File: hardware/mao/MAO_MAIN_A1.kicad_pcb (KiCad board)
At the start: 4 copper layers, 58 x 56 mm, 137 parts, among them J101 USB-C, J102 BAT, J201 TAG, J301 LCD, J501 LRA, Q101 AO3401A, Q302 DMG2302UK, Q501 AO3400A, SW301 SKQGADE010, U101 TPD2E2U06, U102 BQ25185DLHR, U103 MAX17048G+T10, U104 TPS62840DLCR, U105 TPS22916CYFPR, U201 ESP32-S3-MINI-1-N8, U301 DRV5012AEDMRR, U302 DRV5012AEDMRR, U304 TLV9061IDBVR, U401 ICM-42670-P, U402 VL53L4CDV0DH/1, U501 MAX98357AETE+T, U502 DRV2605LDGSR, U503 IRM-H638T/TR2, U504 TPS22916CYFPR

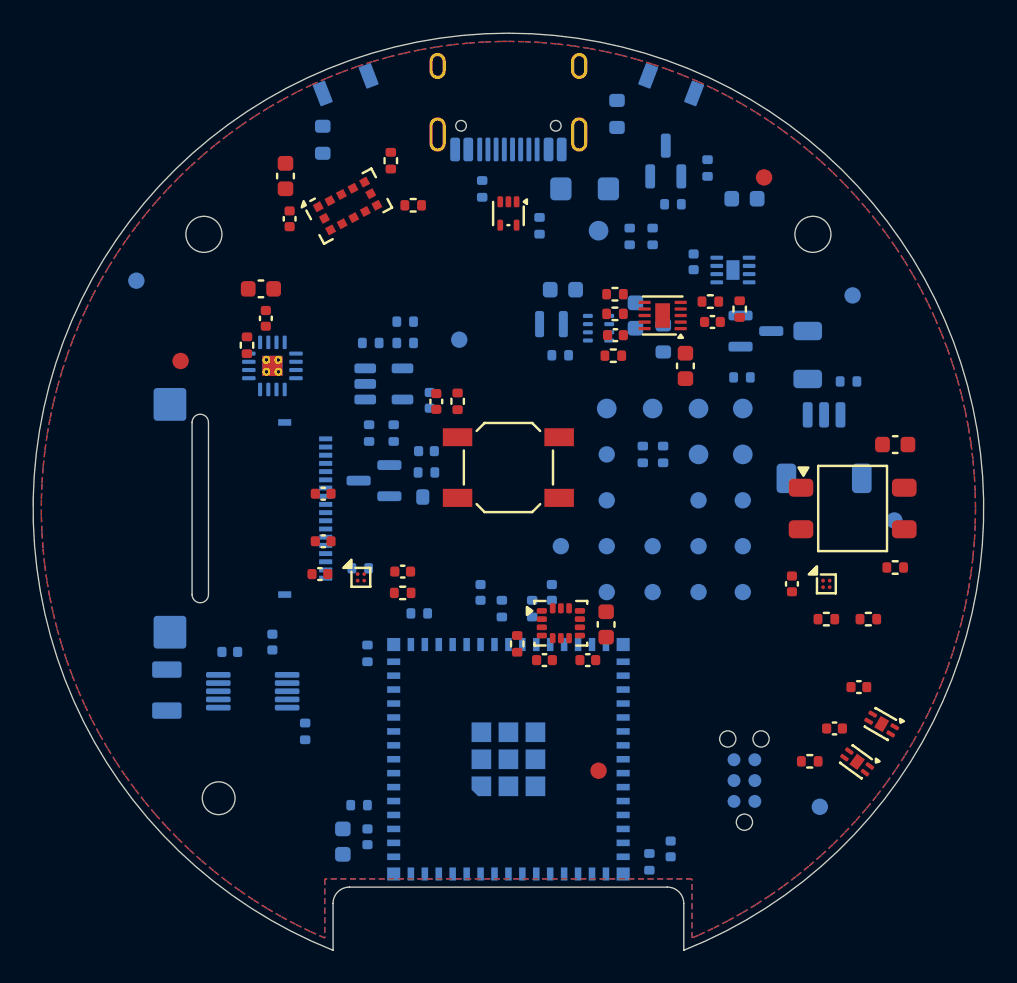
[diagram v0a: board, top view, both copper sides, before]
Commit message: A1 designed copper and rules: BQ25185/TPS62840 power section, VSYS L3 band, A0 copper kept where parts kept
route_power.py / route_local.py rewritten for A1: the buck's input loop, switch node, COUT and VOS sense,
charger SYS to LINK_REG and the L3 VSYS band through two vias, the VSYS via at each load; A0's copper stays for
the USB-C entry, battery chain, speaker, LRA, IR LEDs, ToF, gauge, Hall pair, IR receiver, haptic driver and
service-field pull-ups. power_regions.py: new VSYS band (no 9 o'clock run: the haptic driver is on +3V3) and
+3V3 cores; netrules/project: A1 nets and classes. DRC on the unrouted board: 0 clearance findings.

Co-Authored-By: Claude Opus 5.5 <noreply@anthropic.com>
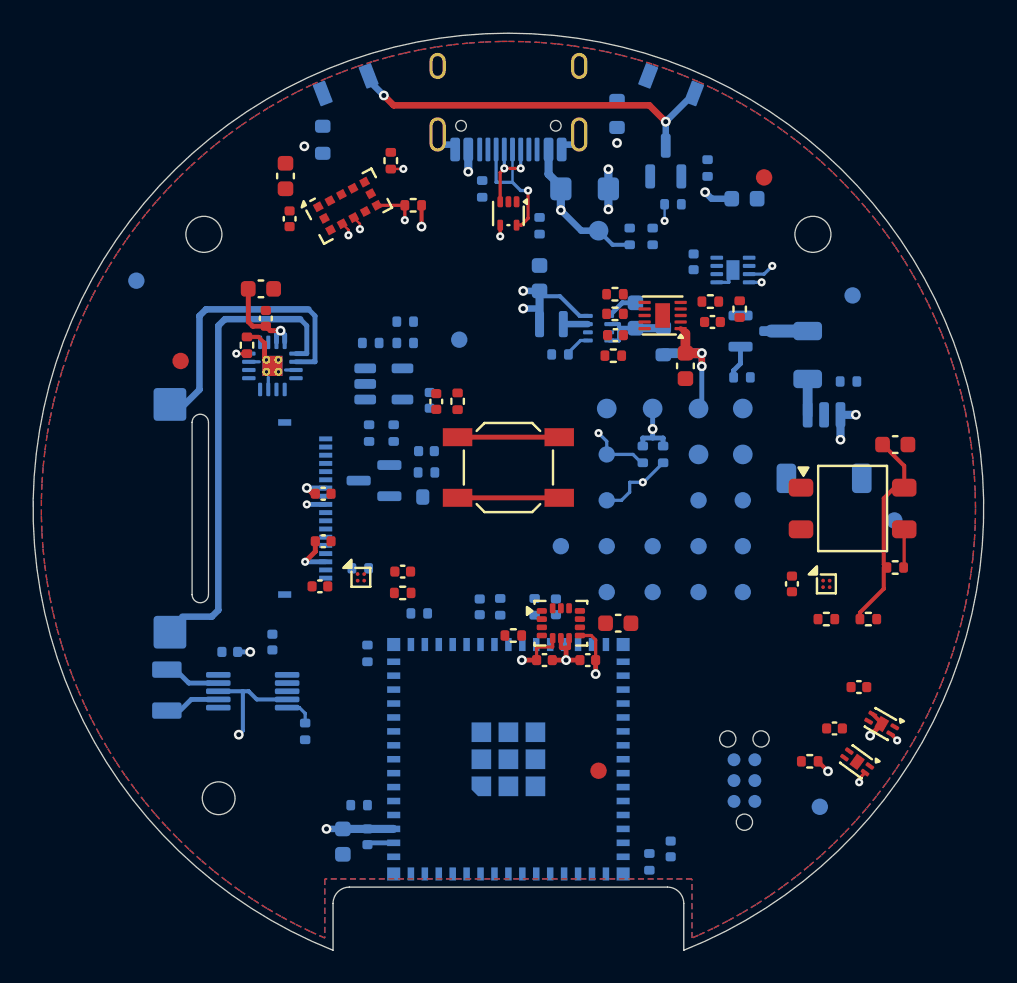
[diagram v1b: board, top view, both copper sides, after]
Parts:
- moved C106 1.59 mm to (51.9, 36.0), turned to 90 degrees
- moved C206 0.91 mm to (52.9, 56.0)
- moved C207 0.88 mm to (48.2, 56.0)
- moved C109 0.75 mm to (38.5, 54.8)
- moved C408 0.74 mm to (56.7, 57.0), turned to 0 degrees
- moved R404 0.56 mm to (50.3, 57.8), turned to 0 degrees
- moved R215 0.19 mm to (51.6, 56.0), turned to -90 degrees
- moved R122 0.17 mm to (59.5, 39.8)
- moved R216 0.15 mm to (49.5, 56.0), turned to -90 degrees
- moved R111 0.05 mm to (53.1, 40.6), turned to 180 degrees
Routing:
- net GND: track 0.00 -> 37.6 mm, vias 0 -> 11
- net SPK_P: track 0.00 -> 27.8 mm
- net +3V3: track 0.00 -> 23.0 mm, vias 0 -> 7
- net IR_LED_K: track 0.00 -> 21.8 mm, vias 0 -> 2
- net VSYS: track 0.00 -> 18.7 mm, vias 0 -> 7
- net SPK_N: track 0.00 -> 17.3 mm
- net IR_RX_VCC: track 0.00 -> 12.2 mm
- net VBUS: track 0.00 -> 9.68 mm, vias 0 -> 2
- net USB_C_DN: track 0.00 -> 7.53 mm, vias 0 -> 1
- net I2C_SCL: track 0.00 -> 6.40 mm, vias 0 -> 3
- net I2C_SDA: track 0.00 -> 6.37 mm, vias 0 -> 3
- net PRESS_N: track 0.00 -> 6.20 mm
- net REG_IN: track 0.00 -> 4.90 mm
- net USB_C_DP: track 0.00 -> 4.24 mm, vias 0 -> 2
- net LRA_N: track 0.00 -> 2.87 mm
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
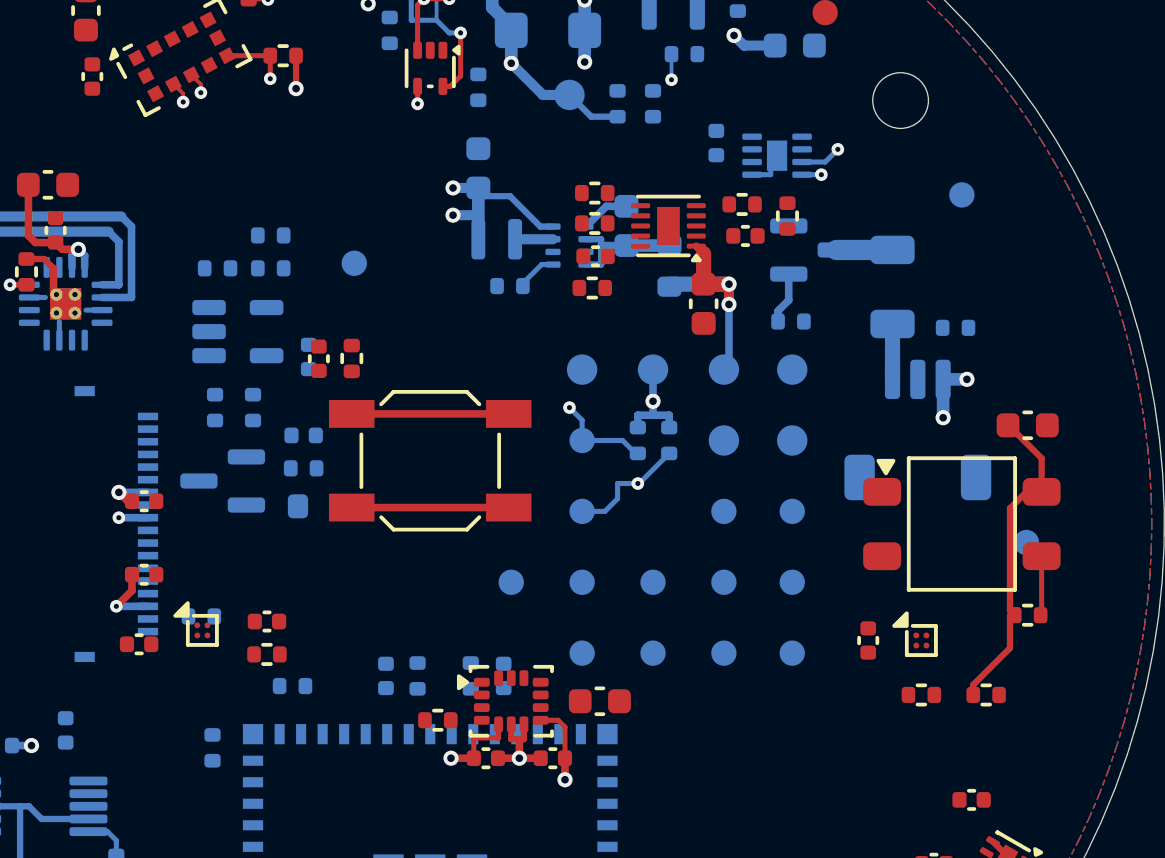
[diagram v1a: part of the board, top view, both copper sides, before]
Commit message: A1 charger fan-out designed (WSON-10 0.4 mm pitch), VBAT chain on B, VSYS strip; A1 power budget
The router could not fan out the BQ25185's 0.4 mm pins: every charger pin now reaches its part on designed
copper, VBAT goes through two vias to Q101, the gauge and TP5 on B, VSYS through two vias to LINK_REG, TP4 and
the L3 band. docs/hardware/mao-power-budget.md is the A1 budget: deep sleep 33.6 uA typ / 66 uA all-max,
+3V3 worst case 543 mA (688 mA by the S3 supply rule) against 750 mA, low-battery floor with the TPS62840 in
100 % mode and Q1's drop.

Co-Authored-By: Claude Opus 5.5 <noreply@anthropic.com>
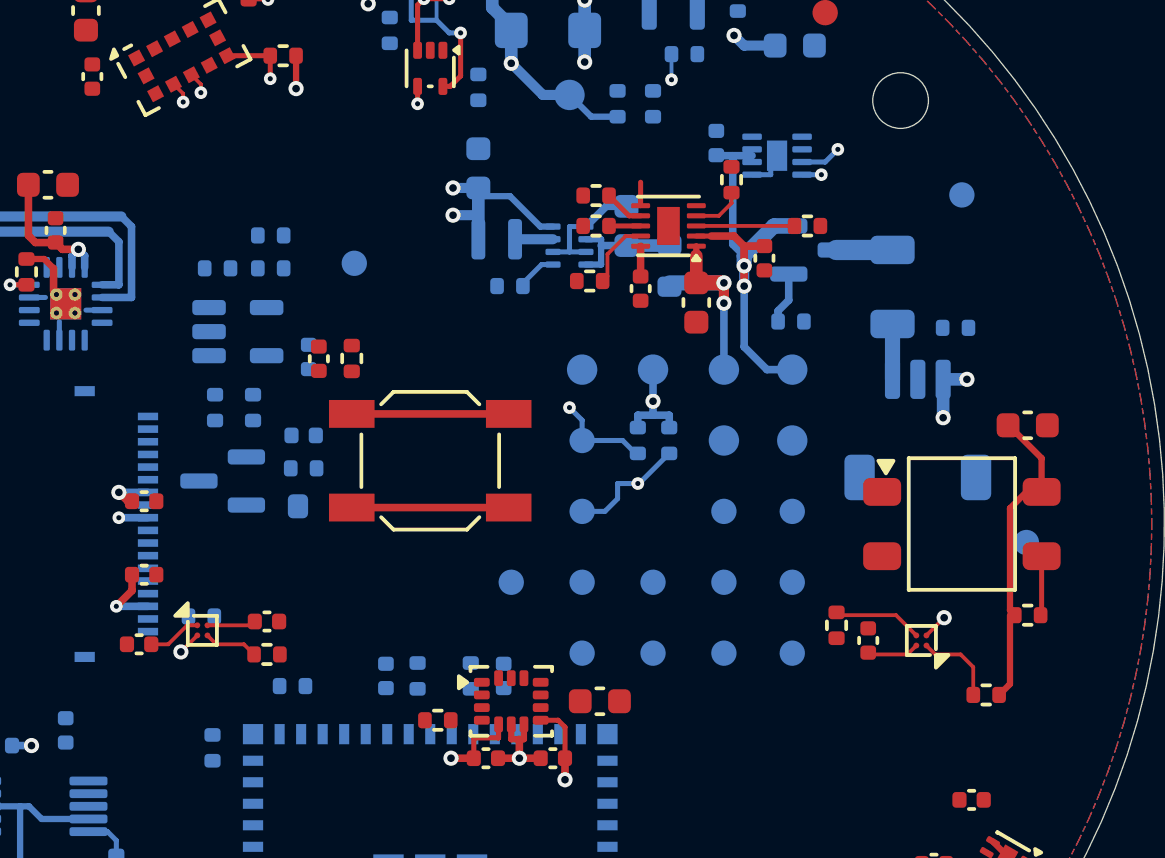
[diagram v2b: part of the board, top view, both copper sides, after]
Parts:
- moved R211 4.33 mm to (66.0, 54.0), turned to -90 degrees
- moved C101 2.19 mm to (58.3, 40.7), turned to -90 degrees
- moved C103 1.16 mm to (63.2, 39.5), turned to -90 degrees
- moved R117 1.06 mm to (61.9, 36.4), turned to 90 degrees
- moved R119 0.88 mm to (64.9, 38.2), turned to 180 degrees
- moved C102 0.29 mm to (60.5, 41.2)
- moved R118 0.29 mm to (56.3, 40.4)
- moved R103 0.11 mm to (56.5, 38.2)
- moved R104 0.11 mm to (56.5, 37.0)
- turned R505 to 0 degrees
- turned U504 to 180 degrees
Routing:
- net VBAT: track 0.00 -> 18.1 mm, vias 0 -> 2
- net GND: track 37.6 -> 42.5 mm, vias 11 -> 13
- net CHG_STAT2: track 0.00 -> 3.88 mm
- net +3V3: track 23.0 -> 26.8 mm
- net AUX_PWR_EN: track 0.00 -> 3.48 mm
- net AUX_3V3: track 0.00 -> 3.30 mm
- net CHG_STAT1: track 0.00 -> 2.74 mm
- net LCD_PWR_EN: track 0.00 -> 2.15 mm
- net 3V3_LCD: track 2.76 -> 4.79 mm
- net CHG_CE_N: track 0.00 -> 2.01 mm
- net CHG_ILIM: track 0.00 -> 1.58 mm
- net CHG_ISET: track 0.00 -> 1.25 mm
- net VBUS: track 9.68 -> 10.9 mm
- net BAT_NTC: track 0.00 -> 0.92 mm

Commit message: A1 layout: module escape vias, J301 DC/TE/RST vias, fixture pads on their nets, BOOT pull-up on F
The first routing pass left 17 connections open around the module: the pin map sends I2S, TE and the dial
across the board, so the crossing pins now leave through staggered escape vias (F and L3 open to the router),
J301's DC/TE/RST drop through vias east of their pads, the display-lane L3 core is gone, and the Gate C fixture
pads sit on their own nets' paths instead of walling off the module's top row. No pin assignment changed.

Co-Authored-By: Claude Opus 5.5 <noreply@anthropic.com>
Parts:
- R202: moved to F.Cu
- moved TP18 26.8 mm to (35.0, 35.7)
- moved TP23 19.4 mm to (59.4, 35.7)
- moved TP17 16.4 mm to (47.0, 37.1)
- moved TP20 14.0 mm to (47.6, 52.4)
- moved TP24 10.3 mm to (51.4, 53.8)
- moved TP25 10.2 mm to (54.2, 53.8)
- moved TP21 9.74 mm to (69.4, 60.6)
- moved R207 9.10 mm to (40.9, 62.8), turned to 180 degrees
- moved TP22 8.76 mm to (64.3, 52.3)
- moved TP19 5.18 mm to (59.7, 57.4)
- moved R202 0.67 mm to (40.6, 68.7)
- moved C301 0.60 mm to (38.1, 52.0)
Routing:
- net LCD_RST_N: track 0.00 -> 3.89 mm, vias 0 -> 1
- net LCD_TE: track 0.00 -> 2.80 mm, vias 0 -> 2
- net LCD_BL_K: track 0.00 -> 2.40 mm
- net LCD_BL: track 0.00 -> 2.00 mm, vias 0 -> 1
- net IMU_INT1: track 0.00 -> 2.00 mm, vias 0 -> 1
- net AMP_DIN: track 0.00 -> 2.00 mm, vias 0 -> 1
- net AMP_BCLK: track 0.00 -> 2.00 mm, vias 0 -> 1
- net LCD_DC: track 0.00 -> 2.00 mm, vias 0 -> 2
- net BOOT: track 0.00 -> 1.89 mm, vias 0 -> 1
- net I2C_SCL: track 6.40 -> 8.06 mm, vias 3 -> 4
- net I2C_SDA: track 6.37 -> 7.96 mm, vias 3 -> 4
- net PRESS_N: track 6.20 -> 7.40 mm, vias 0 -> 1
- net AMP_SD: track 1.41 -> 2.61 mm, vias 1 -> 2
- net AMP_LRCLK: track 0.00 -> 1.20 mm, vias 0 -> 1
- net IR_TX: track 1.01 -> 2.06 mm, vias 1 -> 2

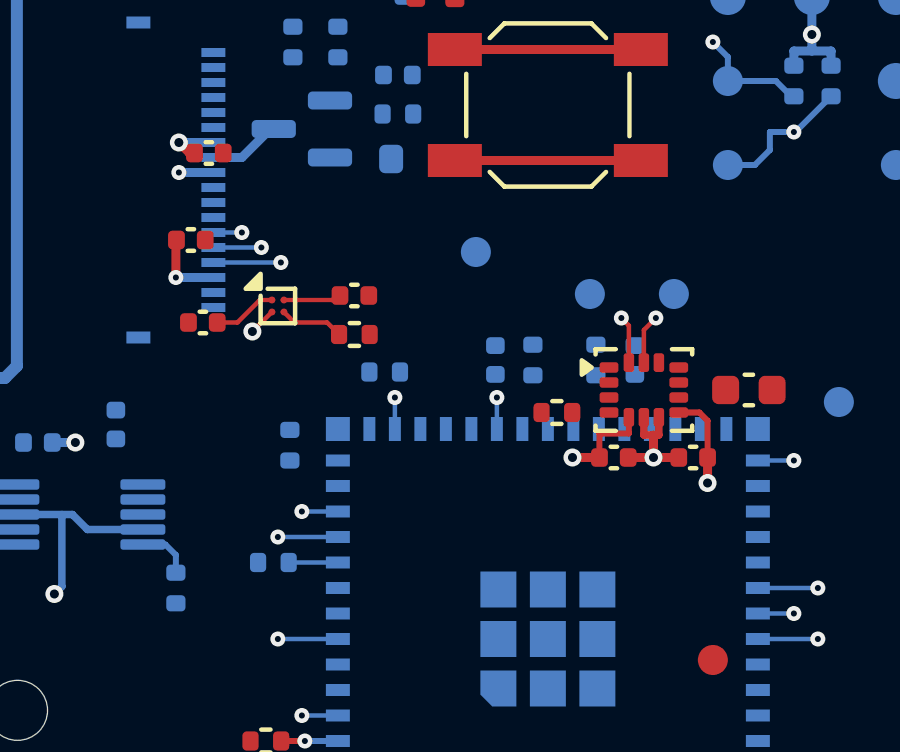
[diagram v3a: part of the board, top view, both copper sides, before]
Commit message: A1 layout: SPI pads of J301 drop to F, USB 22R on F over the module, spare-GPIO pads open
Co-Authored-By: Claude Opus 5.5 <noreply@anthropic.com>
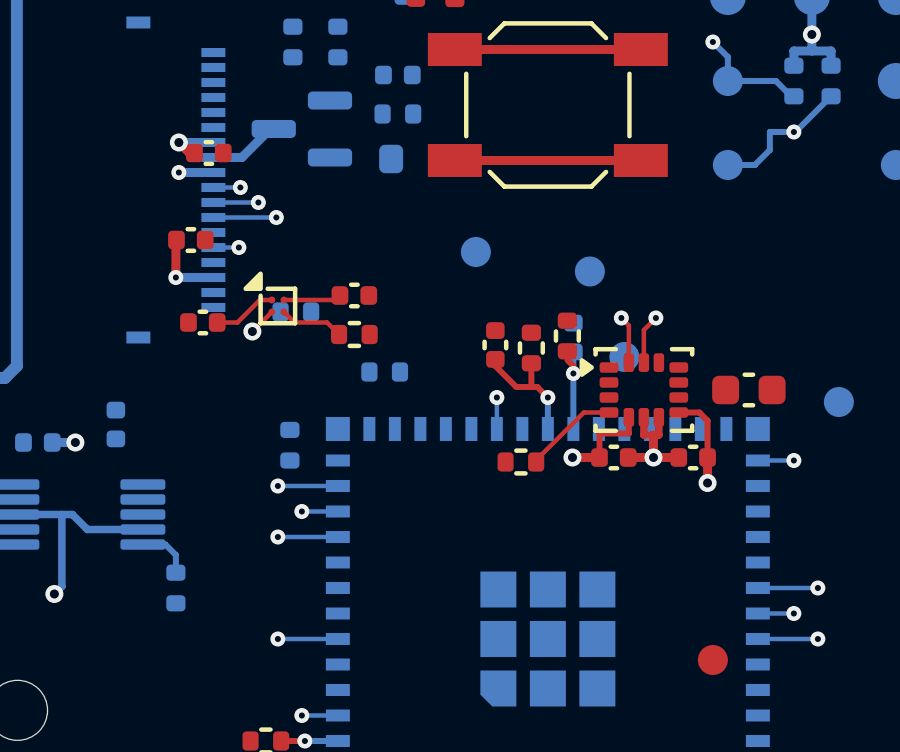
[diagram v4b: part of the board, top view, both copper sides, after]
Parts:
- C207, R215, R216: moved to F.Cu
- moved R207 8.38 mm to (41.6, 54.4), turned to 0 degrees
- moved TP25 2.67 mm to (52.5, 55.9)
- moved C206 2.18 mm to (50.9, 55.2)
- moved R404 2.04 mm to (49.1, 59.4)
- moved R215 1.24 mm to (50.6, 55.2)
- moved TP24 0.75 mm to (51.4, 53.0)
- moved C207 0.50 mm to (48.2, 55.5)
- moved R216 0.40 mm to (49.5, 55.6)
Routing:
- net USB_DN: track 0.00 -> 4.24 mm, vias 0 -> 1
- net LCD_RST_N: track 3.89 -> 0.00 mm, vias 1 -> 0
- net IMU_INT1: track 2.00 -> 5.15 mm
- net USB_DP: track 0.00 -> 3.10 mm, vias 0 -> 1
- net LCD_CS: track 0.00 -> 2.90 mm, vias 0 -> 2
- net LCD_MOSI_P: track 0.00 -> 2.10 mm, vias 0 -> 1
- net LCD_DC: track 2.00 -> 0.00 mm, vias 2 -> 0
- net LCD_SCLK_P: track 0.00 -> 1.50 mm, vias 0 -> 1
- net LCD_TE: track 2.80 -> 2.05 mm

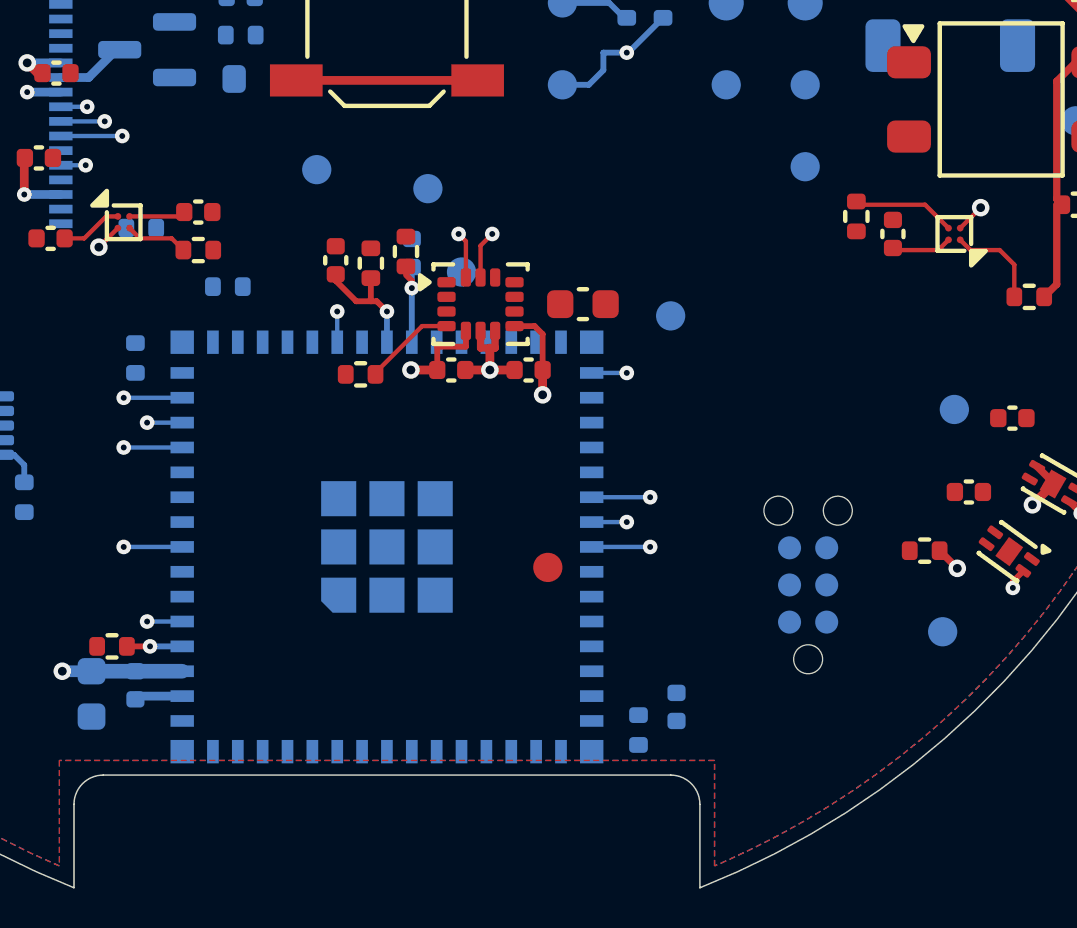
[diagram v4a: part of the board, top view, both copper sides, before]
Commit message: A1 layout: more module escapes, EN corner rebuilt, +3V3 drops where the plane-via search had no site
Co-Authored-By: Claude Opus 5.5 <noreply@anthropic.com>
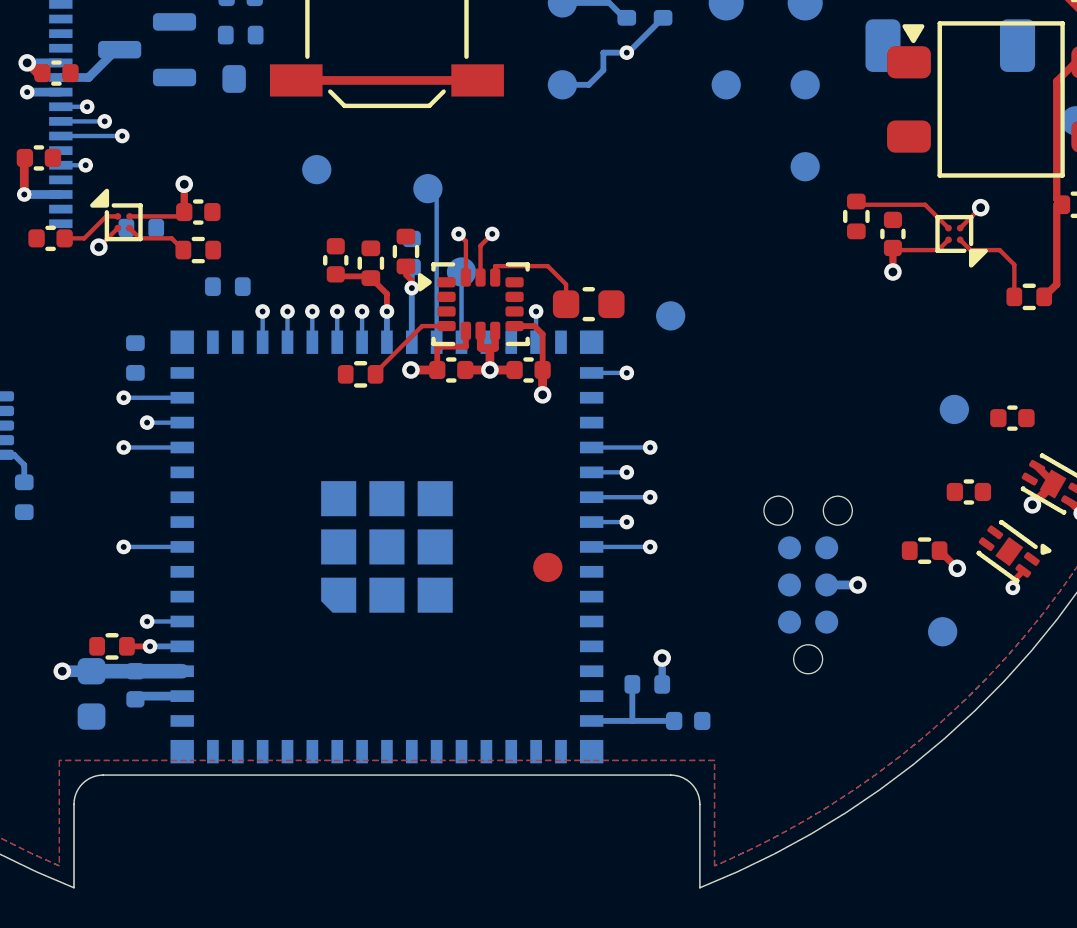
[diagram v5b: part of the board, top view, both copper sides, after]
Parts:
- moved R201 1.59 mm to (58.9, 70.0), turned to 180 degrees
- moved C203 0.62 mm to (60.3, 71.2), turned to 0 degrees
- moved C408 0.20 mm to (56.9, 57.0)
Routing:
- net +3V3: track 26.8 -> 34.3 mm, vias 7 -> 11
- net GPIO21: track 0.00 -> 5.37 mm
- net MCU_EN: track 0.00 -> 4.07 mm
- net GPIO26: track 0.00 -> 2.40 mm
- net TOF_INT_N: track 2.61 -> 4.61 mm, vias 1 -> 2
- net VBUS_SENSE: track 0.00 -> 1.20 mm, vias 0 -> 1
- net TOF_XSHUT: track 0.77 -> 1.82 mm, vias 1 -> 2
- net HAPTIC_EN: track 1.83 -> 2.88 mm, vias 0 -> 1
- net CHG_STAT2: track 3.88 -> 4.93 mm, vias 0 -> 1
- net CHG_CE_N: track 2.01 -> 3.06 mm, vias 0 -> 1
- net AUX_PWR_EN: track 3.48 -> 4.53 mm, vias 0 -> 1
- net USB_DN: track 4.24 -> 3.63 mm
